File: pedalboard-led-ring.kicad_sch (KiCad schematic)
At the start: 30 parts, among them J1 middle, J2 edge

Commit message: Add model for actuator
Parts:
- added H4: Actuator Hole, Library:Actuator, symbol Mechanical:MountingHole
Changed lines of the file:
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@@
+    )
+  )
+  (symbol (lib_id "Mechanical:MountingHole") (at 90.17 185.42 0) (unit 1)
+    (in_bom yes) (on_board yes) (dnp no) (fields_autoplaced)
+    (property "Reference" "H4" (at 92.71 184.785 0)
+      (effects (font (size 1.27 1.27)) (justify left))
+    )
+    (property "Value" "Actuator Hole" (at 92.71 187.325 0)
+      (effects (font (size 1.27 1.27)) (justify left))
+    )
+    (property "Footprint" "Library:Actuator" (at 90.17 185.42 0)
+      (effects (font (size 1.27 1.27)) hide)
+    )
+    (property "Datasheet" "~" (at 90.17 185.42 0)
+      (effects (font (size 1.27 1.27)) hide)
+    )
+    (instances
+      (project "pedalboard-led-ring"
+        (path "/02aefeb1-bdda-4e04-a64a-6cb1fcf66702"
+          (reference "H4") (unit 1)
+        )
+      )
     )
   )

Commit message: Specify the parts
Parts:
- C1, C10, C11, C12, C2, C3, C4, C5, C6, C7, C8, C9: Supplier (none) -> https://www.digikey.ch/en/products/detail/samsung-electro-m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
- D1, D10, D11, D12, D2, D3, D4, D5, D6, D7, D8, D9: Supplier (none) -> https://www.digikey.ch/en/products/detail/adafruit-industri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
- J1, J2: Supplier (none) -> https://www.digikey.ch/en/products/detail/gct/BF100-04-A-D-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; now not fitted
- R1: Supplier (none) -> https://www.digikey.ch/en/products/detail/panasonic-electro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

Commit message: Fix 3d Model for LEDs
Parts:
- D1, D10, D11, D12, D2, D3, D4, D5, D6, D7, D8, D9: value SK6812MINI -> SK6812_EC15; footprint LED_SMD:LED_SK6812_EC15_1.5x1.5mm -> Library:LED_SK6812_EC15_1.5x1.5mm
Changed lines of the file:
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@@
       (effects (font (size 1.27 1.27)))
     )
-    (property "Value" "SK6812MINI" (at 88.9 50.2159 0)
-      (effects (font (size 1.27 1.27)) hide)
-    )
-    (property "Footprint" "LED_SMD:LED_SK6812_EC15_1.5x1.5mm" (at 77.47 58.42 0)
+    (property "Value" "SK6812_EC15" (at 88.9 50.2159 0)
+      (effects (font (size 1.27 1.27)) hide)
+    )
+    (property "Footprint" "Library:LED_SK6812_EC15_1.5x1.5mm" (at 77.47 58.42 0)
       (effects (font (size 1.27 1.27)) (justify left top) hide)
     )
@@
       (effects (font (size 1.27 1.27)))
     )
-    (property "Value" "SK6812MINI" (at 160.02 50.2159 0)
-      (effects (font (size 1.27 1.27)) hide)
-    )
-    (property "Footprint" "LED_SMD:LED_SK6812_EC15_1.5x1.5mm" (at 148.59 58.42 0)
+    (property "Value" "SK6812_EC15" (at 160.02 50.2159 0)
+      (effects (font (size 1.27 1.27)) hide)
+    )
+    (property "Footprint" "Library:LED_SK6812_EC15_1.5x1.5mm" (at 148.59 58.42 0)
       (effects (font (size 1.27 1.27)) (justify left top) hide)
     )
@@
       (effects (font (size 1.27 1.27)))
     )
-    (property "Value" "SK6812MINI" (at 177.8 50.2159 0)
-      (effects (font (size 1.27 1.27)) hide)
-    )
-    (property "Footprint" "LED_SMD:LED_SK6812_EC15_1.5x1.5mm" (at 166.37 58.42 0)
+    (property "Value" "SK6812_EC15" (at 177.8 50.2159 0)
+      (effects (font (size 1.27 1.27)) hide)
+    )
+    (property "Footprint" "Library:LED_SK6812_EC15_1.5x1.5mm" (at 166.37 58.42 0)
       (effects (font (size 1.27 1.27)) (justify left top) hide)
     )
@@
       (effects (font (size 1.27 1.27)))
     )
-    (property "Value" "SK6812MINI" (at 124.46 50.2159 0)
-      (effects (font (size 1.27 1.27)) hide)
-    )
-    (property "Footprint" "LED_SMD:LED_SK6812_EC15_1.5x1.5mm" (at 113.03 58.42 0)
+    (property "Value" "SK6812_EC15" (at 124.46 50.2159 0)
+      (effects (font (size 1.27 1.27)) hide)
+    )
+    (property "Footprint" "Library:LED_SK6812_EC15_1.5x1.5mm" (at 113.03 58.42 0)
       (effects (font (size 1.27 1.27)) (justify left top) hide)
     )
@@
       (effects (font (size 1.27 1.27)))
     )
-    (property "Value" "SK6812MINI" (at 213.36 50.2159 0)
-      (effects (font (size 1.27 1.27)) hide)
-    )
-    (property "Footprint" "LED_SMD:LED_SK6812_EC15_1.5x1.5mm" (at 201.93 58.42 0)
+    (property "Value" "SK6812_EC15" (at 213.36 50.2159 0)
+      (effects (font (size 1.27 1.27)) hide)
+    )
+    (property "Footprint" "Library:LED_SK6812_EC15_1.5x1.5mm" (at 201.93 58.42 0)
       (effects (font (size 1.27 1.27)) (justify left top) hide)
     )
@@
       (effects (font (size 1.27 1.27)))
     )
-    (property "Value" "SK6812MINI" (at 49.53 43.18 0)
-      (effects (font (size 1.27 1.27)) hide)
-    )
-    (property "Footprint" "LED_SMD:LED_SK6812_EC15_1.5x1.5mm" (at 41.91 58.42 0)
+    (property "Value" "SK6812_EC15" (at 49.53 43.18 0)
+      (effects (font (size 1.27 1.27)) hide)
+    )
+    (property "Footprint" "Library:LED_SK6812_EC15_1.5x1.5mm" (at 41.91 58.42 0)
       (effects (font (size 1.27 1.27)) (justify left top) hide)
     )
@@
       (effects (font (size 1.27 1.27)))
     )
-    (property "Value" "SK6812MINI" (at 71.12 50.2159 0)
-      (effects (font (size 1.27 1.27)) hide)
-    )
-    (property "Footprint" "LED_SMD:LED_SK6812_EC15_1.5x1.5mm" (at 59.69 58.42 0)
+    (property "Value" "SK6812_EC15" (at 71.12 50.2159 0)
+      (effects (font (size 1.27 1.27)) hide)
+    )
+    (property "Footprint" "Library:LED_SK6812_EC15_1.5x1.5mm" (at 59.69 58.42 0)
       (effects (font (size 1.27 1.27)) (justify left top) hide)
     )
@@
       (effects (font (size 1.27 1.27)))
     )
-    (property "Value" "SK6812MINI" (at 195.58 50.2159 0)
-      (effects (font (size 1.27 1.27)) hide)
-    )
-    (property "Footprint" "LED_SMD:LED_SK6812_EC15_1.5x1.5mm" (at 184.15 58.42 0)
+    (property "Value" "SK6812_EC15" (at 195.58 50.2159 0)
+      (effects (font (size 1.27 1.27)) hide)
+    )
+    (property "Footprint" "Library:LED_SK6812_EC15_1.5x1.5mm" (at 184.15 58.42 0)
       (effects (font (size 1.27 1.27)) (justify left top) hide)
     )
@@
       (effects (font (size 1.27 1.27)))
     )
-    (property "Value" "SK6812MINI" (at 106.68 50.2159 0)
-      (effects (font (size 1.27 1.27)) hide)
-    )
-    (property "Footprint" "LED_SMD:LED_SK6812_EC15_1.5x1.5mm" (at 95.25 58.42 0)
+    (property "Value" "SK6812_EC15" (at 106.68 50.2159 0)
+      (effects (font (size 1.27 1.27)) hide)
+    )
+    (property "Footprint" "Library:LED_SK6812_EC15_1.5x1.5mm" (at 95.25 58.42 0)
       (effects (font (size 1.27 1.27)) (justify left top) hide)
     )
@@
       (effects (font (size 1.27 1.27)))
     )
-    (property "Value" "SK6812MINI" (at 248.92 50.2159 0)
-      (effects (font (size 1.27 1.27)) hide)
-    )
-    (property "Footprint" "LED_SMD:LED_SK6812_EC15_1.5x1.5mm" (at 237.49 58.42 0)
+    (property "Value" "SK6812_EC15" (at 248.92 50.2159 0)
+      (effects (font (size 1.27 1.27)) hide)
+    )
+    (property "Footprint" "Library:LED_SK6812_EC15_1.5x1.5mm" (at 237.49 58.42 0)
       (effects (font (size 1.27 1.27)) (justify left top) hide)
     )
@@
       (effects (font (size 1.27 1.27)))
     )
-    (property "Value" "SK6812MINI" (at 231.14 50.2159 0)
-      (effects (font (size 1.27 1.27)) hide)
-    )
-    (property "Footprint" "LED_SMD:LED_SK6812_EC15_1.5x1.5mm" (at 219.71 58.42 0)
+    (property "Value" "SK6812_EC15" (at 231.14 50.2159 0)
+      (effects (font (size 1.27 1.27)) hide)
+    )
+    (property "Footprint" "Library:LED_SK6812_EC15_1.5x1.5mm" (at 219.71 58.42 0)
       (effects (font (size 1.27 1.27)) (justify left top) hide)
     )
@@
       (effects (font (size 1.27 1.27)))
     )
-    (property "Value" "SK6812MINI" (at 142.24 50.2159 0)
-      (effects (font (size 1.27 1.27)) hide)
-    )
-    (property "Footprint" "LED_SMD:LED_SK6812_EC15_1.5x1.5mm" (at 130.81 58.42 0)
-      (effects (font (size 1.27 1.27)) (justify left top) hide)
-    )
+    (property "Value" "SK6812_EC15" (at 142.24 50.2159 0)
+      (effects (font (size 1.27 1.27)) hide)
+    )
+    (property "Footprint" "Library:LED_SK6812_EC15_1.5x1.5mm" (at 130.81 58.42 0)
+      (effects (font (size 1.27 1.27)) (justify left top) hide)
+    )

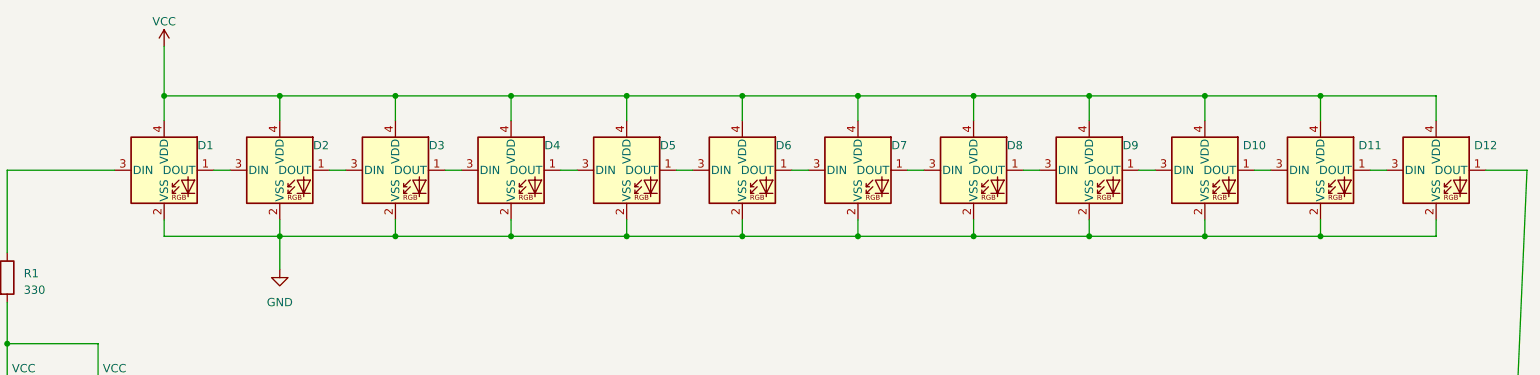
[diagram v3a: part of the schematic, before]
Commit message: Fix the schematic of the Neopixels
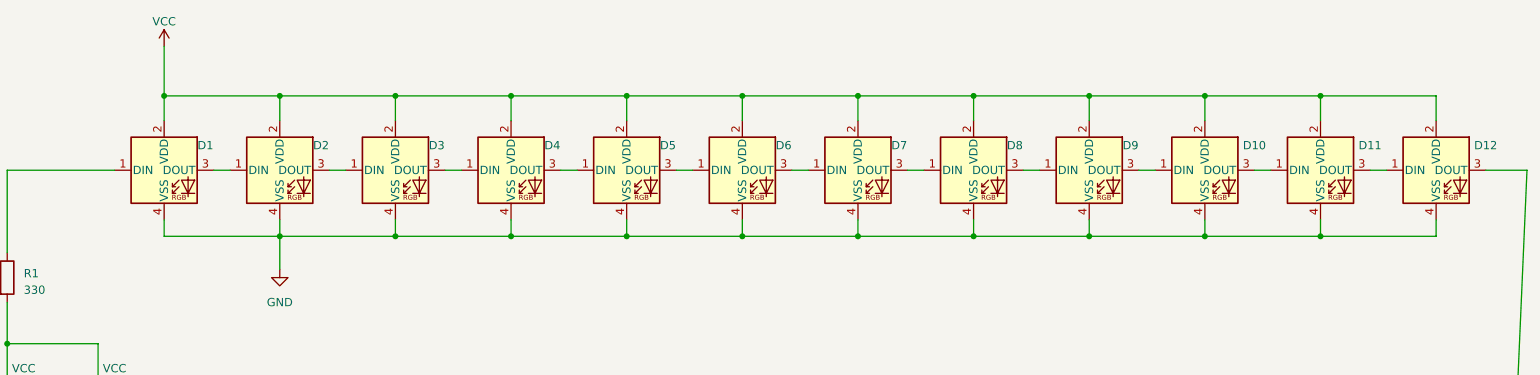
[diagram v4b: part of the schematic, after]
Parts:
- D1, D10, D11, D12, D2, D3, D4, D5, D6, D7, D8, D9: symbol LED:SK6812MINI -> pedalboard-led-ring:SK6812
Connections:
- net GND: now also D1.4 (VSS), D10.4 (VSS), D11.4 (VSS), D12.4 (VSS), D2.4 (VSS), D3.4 (VSS), D4.4 (VSS), D5.4 (VSS), D6.4 (VSS), D7.4 (VSS), D8.4 (VSS), D9.4 (VSS); no longer D1.2 (VSS), D10.2 (VSS), D11.2 (VSS), D12.2 (VSS), D2.2 (VSS), D3.2 (VSS), D4.2 (VSS), D5.2 (VSS), D6.2 (VSS), D7.2 (VSS), D8.2 (VSS), D9.2 (VSS)
- net VCC: now also D1.2 (VDD), D10.2 (VDD), D11.2 (VDD), D12.2 (VDD), D2.2 (VDD), D3.2 (VDD), D4.2 (VDD), D5.2 (VDD), D6.2 (VDD), D7.2 (VDD), D8.2 (VDD), D9.2 (VDD); no longer D1.4 (VDD), D10.4 (VDD), D11.4 (VDD), D12.4 (VDD), D2.4 (VDD), D3.4 (VDD), D4.4 (VDD), D5.4 (VDD), D6.4 (VDD), D7.4 (VDD), D8.4 (VDD), D9.4 (VDD)
- net at D3.1 (DIN): now also D2.3 (DOUT); no longer D4.3 (DIN)
- net at D3.3 (DOUT): now also D4.1 (DIN); no longer D2.1 (DOUT)
- net at D7.1 (DIN): now also D6.3 (DOUT); no longer D8.3 (DIN)
- net at D7.3 (DOUT): now also D8.1 (DIN); no longer D6.1 (DOUT)
- net at D9.3 (DOUT): now also D10.1 (DIN); no longer D8.1 (DOUT)
- net at J1.4 (Pin_4), J2.4 (Pin_4): now also D12.3 (DOUT); no longer D12.1 (DOUT)
- net at D5.1 (DIN): now also D4.3 (DOUT); no longer D6.3 (DIN)
- net at D5.3 (DOUT): now also D6.1 (DIN); no longer D4.1 (DOUT)
- net at D11.3 (DOUT): now also D12.1 (DIN); no longer D10.1 (DOUT)
- net at D9.1 (DIN): now also D8.3 (DOUT); no longer D10.3 (DIN)
- net at R1.1: now also D1.1 (DIN); no longer D1.3 (DIN)
- net at D11.1 (DIN): now also D10.3 (DOUT); no longer D12.3 (DIN)
- new net: D1.3 (DOUT), D2.1 (DIN)
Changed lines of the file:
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@@
     )
   )
-  (symbol (lib_id "LED:SK6812MINI") (at 76.2 50.8 0) (unit 1)
+  (symbol (lib_id "pedalboard-led-ring:SK6812") (at 76.2 50.8 0) (unit 1)
     (in_bom yes) (on_board yes) (dnp no)
     (property "Reference" "D3" (at 82.55 46.99 0)
@@
       (effects (font (size 1.27 1.27)) (justify left top) hide)
     )
-    (property "Datasheet" "https://cdn-shop.adafruit.com/product-files/4492/Datasheet.pdf" (at 78.74 60.325 0)
+    (property "Datasheet" "https://cdn-shop.adafruit.com/product-files/1138/SK6812+LED+datasheet+.pdf" (at 78.74 60.325 0)
       (effects (font (size 1.27 1.27)) (justify left top) hide)
     )
@@
     )
   )
-  (symbol (lib_id "LED:SK6812MINI") (at 147.32 50.8 0) (unit 1)
+  (symbol (lib_id "pedalboard-led-ring:SK6812") (at 147.32 50.8 0) (unit 1)
     (in_bom yes) (on_board yes) (dnp no)
     (property "Reference" "D7" (at 153.67 46.99 0)
@@
       (effects (font (size 1.27 1.27)) (justify left top) hide)
     )
-    (property "Datasheet" "https://cdn-shop.adafruit.com/product-files/4492/Datasheet.pdf" (at 149.86 60.325 0)
+    (property "Datasheet" "https://cdn-shop.adafruit.com/product-files/1138/SK6812+LED+datasheet+.pdf" (at 149.86 60.325 0)
       (effects (font (size 1.27 1.27)) (justify left top) hide)
     )
@@
     )
   )
-  (symbol (lib_id "LED:SK6812MINI") (at 165.1 50.8 0) (unit 1)
+  (symbol (lib_id "pedalboard-led-ring:SK6812") (at 165.1 50.8 0) (unit 1)
     (in_bom yes) (on_board yes) (dnp no)
     (property "Reference" "D8" (at 171.45 46.99 0)
@@
       (effects (font (size 1.27 1.27)) (justify left top) hide)
     )
-    (property "Datasheet" "https://cdn-shop.adafruit.com/product-files/4492/Datasheet.pdf" (at 167.64 60.325 0)
+    (property "Datasheet" "https://cdn-shop.adafruit.com/product-files/1138/SK6812+LED+datasheet+.pdf" (at 167.64 60.325 0)
       (effects (font (size 1.27 1.27)) (justify left top) hide)
     )
@@
     )
   )
-  (symbol (lib_id "LED:SK6812MINI") (at 111.76 50.8 0) (unit 1)
+  (symbol (lib_id "pedalboard-led-ring:SK6812") (at 111.76 50.8 0) (unit 1)
     (in_bom yes) (on_board yes) (dnp no)
     (property "Reference" "D5" (at 118.11 46.99 0)
@@
       (effects (font (size 1.27 1.27)) (justify left top) hide)
     )
-    (property "Datasheet" "https://cdn-shop.adafruit.com/product-files/4492/Datasheet.pdf" (at 114.3 60.325 0)
+    (property "Datasheet" "https://cdn-shop.adafruit.com/product-files/1138/SK6812+LED+datasheet+.pdf" (at 114.3 60.325 0)
       (effects (font (size 1.27 1.27)) (justify left top) hide)
     )
@@
     )
   )
-  (symbol (lib_id "LED:SK6812MINI") (at 200.66 50.8 0) (unit 1)
+  (symbol (lib_id "pedalboard-led-ring:SK6812") (at 200.66 50.8 0) (unit 1)
     (in_bom yes) (on_board yes) (dnp no)
     (property "Reference" "D10" (at 208.28 46.99 0)
@@
       (effects (font (size 1.27 1.27)) (justify left top) hide)
     )
-    (property "Datasheet" "https://cdn-shop.adafruit.com/product-files/4492/Datasheet.pdf" (at 203.2 60.325 0)
+    (property "Datasheet" "https://cdn-shop.adafruit.com/product-files/1138/SK6812+LED+datasheet+.pdf" (at 203.2 60.325 0)
       (effects (font (size 1.27 1.27)) (justify left top) hide)
     )
@@
     )
   )
-  (symbol (lib_id "LED:SK6812MINI") (at 40.64 50.8 0) (unit 1)
+  (symbol (lib_id "pedalboard-led-ring:SK6812") (at 40.64 50.8 0) (unit 1)
     (in_bom yes) (on_board yes) (dnp no)
     (property "Reference" "D1" (at 46.99 46.99 0)
@@
       (effects (font (size 1.27 1.27)) (justify left top) hide)
     )
-    (property "Datasheet" "https://cdn-shop.adafruit.com/product-files/4492/Datasheet.pdf" (at 43.18 60.325 0)
+    (property "Datasheet" "https://cdn-shop.adafruit.com/product-files/1138/SK6812+LED+datasheet+.pdf" (at 43.18 60.325 0)
       (effects (font (size 1.27 1.27)) (justify left top) hide)
     )
@@
     )
   )
-  (symbol (lib_id "LED:SK6812MINI") (at 58.42 50.8 0) (unit 1)
+  (symbol (lib_id "pedalboard-led-ring:SK6812") (at 58.42 50.8 0) (unit 1)
     (in_bom yes) (on_board yes) (dnp no)
     (property "Reference" "D2" (at 64.77 46.99 0)
@@
       (effects (font (size 1.27 1.27)) (justify left top) hide)
     )
-    (property "Datasheet" "https://cdn-shop.adafruit.com/product-files/4492/Datasheet.pdf" (at 60.96 60.325 0)
+    (property "Datasheet" "https://cdn-shop.adafruit.com/product-files/1138/SK6812+LED+datasheet+.pdf" (at 60.96 60.325 0)
       (effects (font (size 1.27 1.27)) (justify left top) hide)
     )
@@
     )
   )
-  (symbol (lib_id "LED:SK6812MINI") (at 182.88 50.8 0) (unit 1)
+  (symbol (lib_id "pedalboard-led-ring:SK6812") (at 182.88 50.8 0) (unit 1)
     (in_bom yes) (on_board yes) (dnp no)
     (property "Reference" "D9" (at 189.23 46.99 0)
@@
       (effects (font (size 1.27 1.27)) (justify left top) hide)
     )
-    (property "Datasheet" "https://cdn-shop.adafruit.com/product-files/4492/Datasheet.pdf" (at 185.42 60.325 0)
+    (property "Datasheet" "https://cdn-shop.adafruit.com/product-files/1138/SK6812+LED+datasheet+.pdf" (at 185.42 60.325 0)
       (effects (font (size 1.27 1.27)) (justify left top) hide)
     )
@@
     )
   )
-  (symbol (lib_id "LED:SK6812MINI") (at 93.98 50.8 0) (unit 1)
+  (symbol (lib_id "pedalboard-led-ring:SK6812") (at 93.98 50.8 0) (unit 1)
     (in_bom yes) (on_board yes) (dnp no)
     (property "Reference" "D4" (at 100.33 46.99 0)
@@
       (effects (font (size 1.27 1.27)) (justify left top) hide)
     )
-    (property "Datasheet" "https://cdn-shop.adafruit.com/product-files/4492/Datasheet.pdf" (at 96.52 60.325 0)
+    (property "Datasheet" "https://cdn-shop.adafruit.com/product-files/1138/SK6812+LED+datasheet+.pdf" (at 96.52 60.325 0)
       (effects (font (size 1.27 1.27)) (justify left top) hide)
     )
@@
     )
   )
-  (symbol (lib_id "LED:SK6812MINI") (at 236.22 50.8 0) (unit 1)
+  (symbol (lib_id "pedalboard-led-ring:SK6812") (at 236.22 50.8 0) (unit 1)
     (in_bom yes) (on_board yes) (dnp no)
     (property "Reference" "D12" (at 243.84 46.99 0)
@@
       (effects (font (size 1.27 1.27)) (justify left top) hide)
     )
-    (property "Datasheet" "https://cdn-shop.adafruit.com/product-files/4492/Datasheet.pdf" (at 238.76 60.325 0)
+    (property "Datasheet" "https://cdn-shop.adafruit.com/product-files/1138/SK6812+LED+datasheet+.pdf" (at 238.76 60.325 0)
       (effects (font (size 1.27 1.27)) (justify left top) hide)
     )
@@
     )
   )
-  (symbol (lib_id "LED:SK6812MINI") (at 218.44 50.8 0) (unit 1)
+  (symbol (lib_id "pedalboard-led-ring:SK6812") (at 218.44 50.8 0) (unit 1)
     (in_bom yes) (on_board yes) (dnp no)
     (property "Reference" "D11" (at 226.06 46.99 0)
@@
       (effects (font (size 1.27 1.27)) (justify left top) hide)
     )
-    (property "Datasheet" "https://cdn-shop.adafruit.com/product-files/4492/Datasheet.pdf" (at 220.98 60.325 0)
+    (property "Datasheet" "https://cdn-shop.adafruit.com/product-files/1138/SK6812+LED+datasheet+.pdf" (at 220.98 60.325 0)
       (effects (font (size 1.27 1.27)) (justify left top) hide)
     )
@@
     )
   )
-  (symbol (lib_id "LED:SK6812MINI") (at 129.54 50.8 0) (unit 1)
+  (symbol (lib_id "pedalboard-led-ring:SK6812") (at 129.54 50.8 0) (unit 1)
     (in_bom yes) (on_board yes) (dnp no)
     (property "Reference" "D6" (at 135.89 46.99 0)
@@
       (effects (font (size 1.27 1.27)) (justify left top) hide)
     )
-    (property "Datasheet" "https://cdn-shop.adafruit.com/product-files/4492/Datasheet.pdf" (at 132.08 60.325 0)
-      (effects (font (size 1.27 1.27)) (justify left top) hide)
-    )
+    (property "Datasheet" "https://cdn-shop.adafruit.com/product-files/1138/SK6812+LED+datasheet+.pdf" (at 132.08 60.325 0)
+      (effects (font (size 1.27 1.27)) (justify left top) hide)
+    )
